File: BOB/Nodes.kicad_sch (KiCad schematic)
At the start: 4 parts, among them J2 Conn_01x18, J5 Conn_01x18, J6 Conn_01x18, J7 Conn_01x18

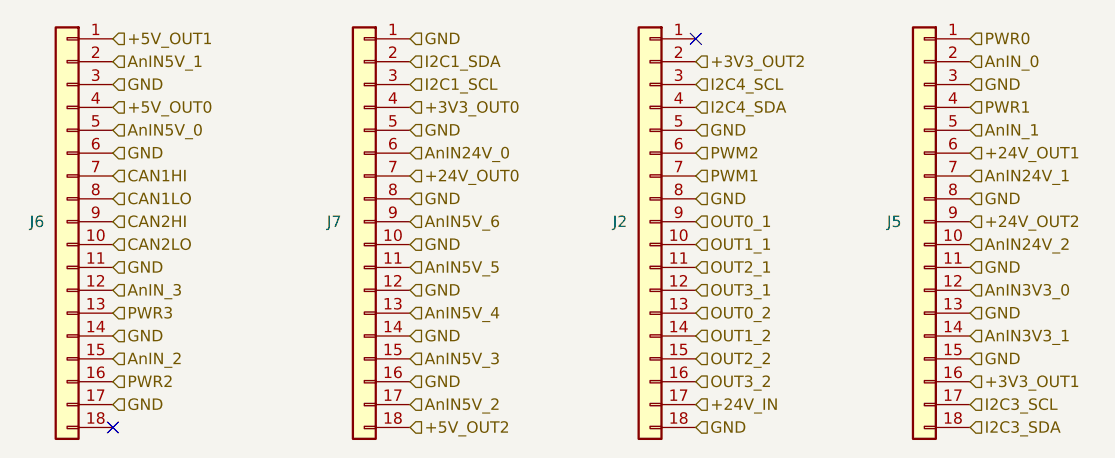
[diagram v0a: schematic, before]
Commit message: BOB v2.1.2
- Reduced font size
- Fixed mistake with CAN numbers
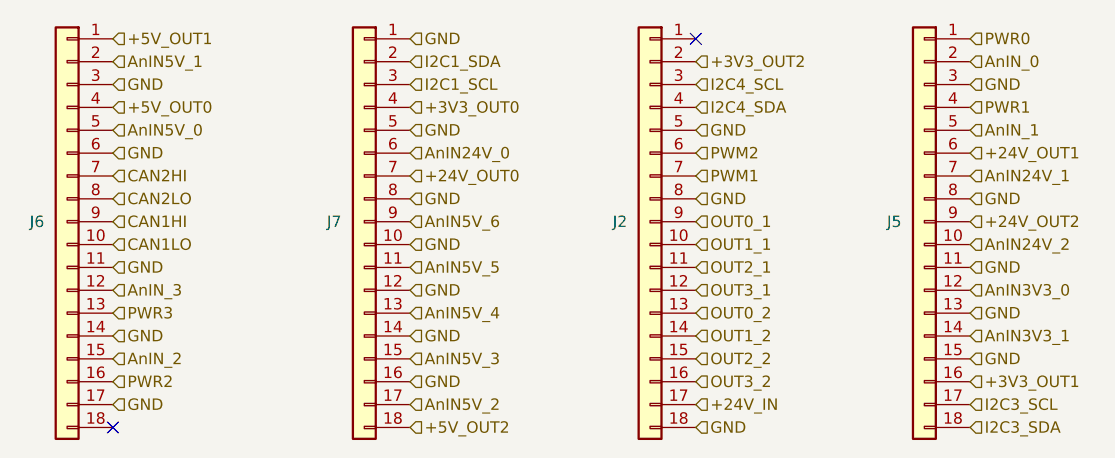
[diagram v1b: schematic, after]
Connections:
- net CAN1HI: now also J6.9 (Pin_9); no longer J6.7 (Pin_7)
- net CAN1LO: now also J6.10 (Pin_10); no longer J6.8 (Pin_8)
- net CAN2HI: now also J6.7 (Pin_7); no longer J6.9 (Pin_9)
- net CAN2LO: now also J6.8 (Pin_8); no longer J6.10 (Pin_10)
